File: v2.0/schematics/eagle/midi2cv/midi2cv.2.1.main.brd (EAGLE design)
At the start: 100 x 41.9 mm, 27 parts, among them IC2 PIC18F2431DIP, Q1 20MHz, X1 MAB5SH

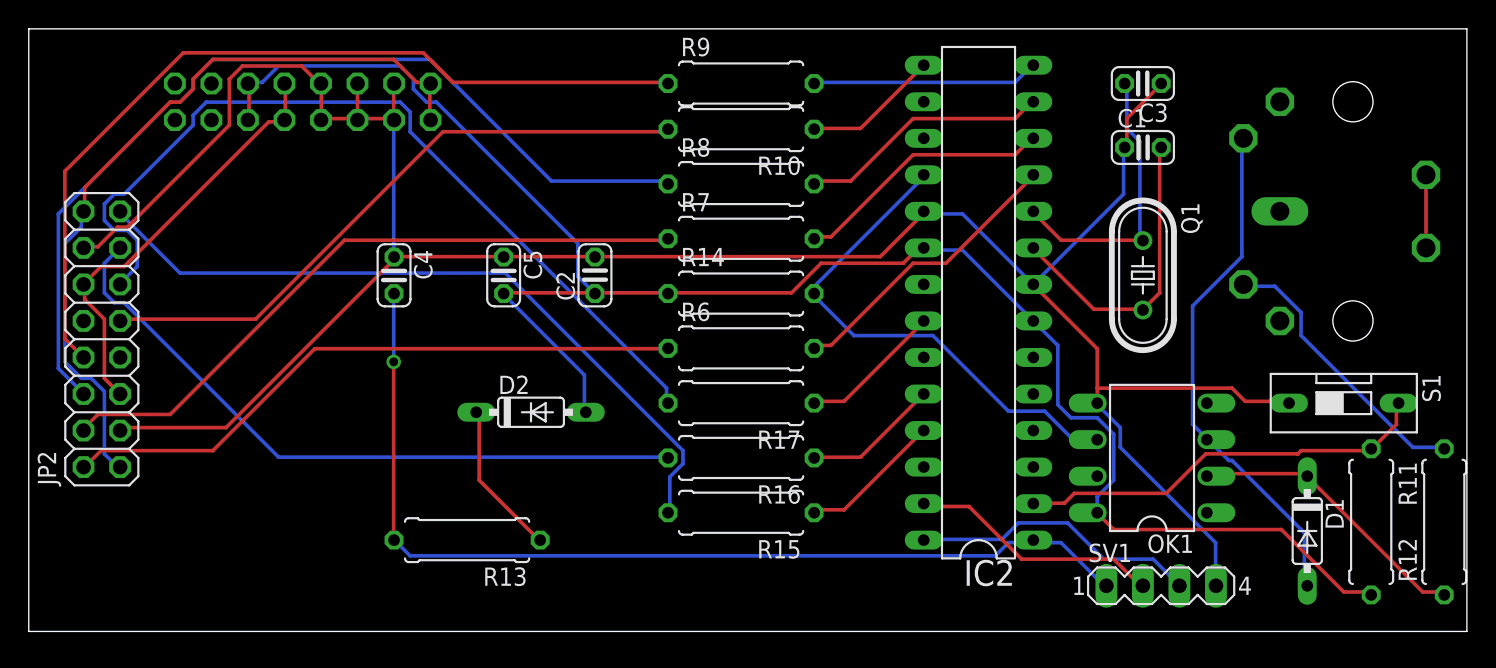
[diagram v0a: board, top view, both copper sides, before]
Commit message: Gerbers generated for midi2cv seeed submission (main and pnl)
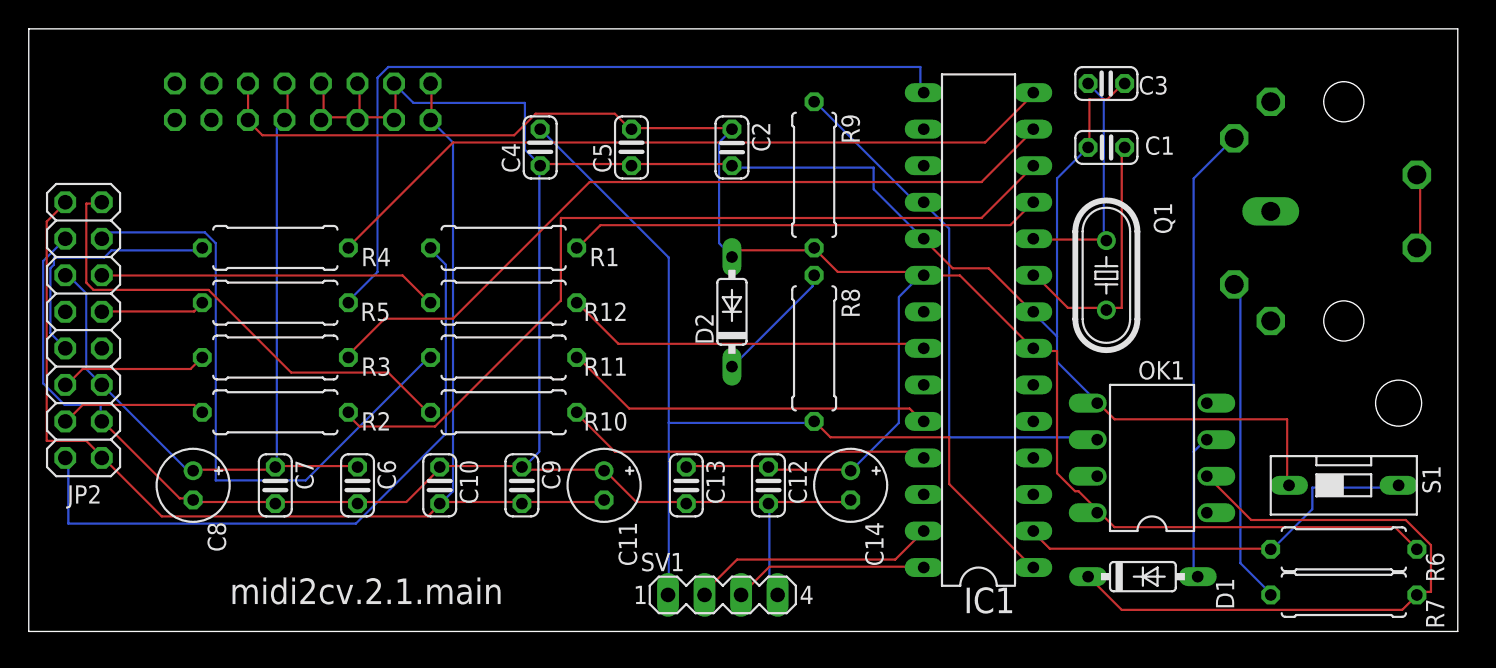
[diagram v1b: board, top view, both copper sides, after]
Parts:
- removed IC2: PIC18F2431DIP, _common:DIL28-3
- removed R13: 10K, _common:0309/10
- removed R14: 360, _common:0309/10
- removed R15, R16, R17: 390, _common:0309/10
- added C10, C13, C7: 0.1uF, _common:C025-024X044
- added C11, C8: 10uF, _common:E2-5
- added C12, C6, C9: 0.01uF, _common:C025-024X044
- added C14: 2.2uF, _common:E2-5
- added IC1: PIC18F2431DIP, _common:DIL28-3
- added R1, R2, R3, R4, R5: 390, _common:0309/10
- R11: value 10K -> 390
- R12: value 220 -> 390
- R6, R8: value 390 -> 10K
- R7: value 390 -> 220
- R9: value 390 -> 360
- moved R12 67.2 mm to (33.0, 22.9), turned to 180 degrees
- moved R11 61.4 mm to (33.0, 19.1), turned to 180 degrees
- moved R7 48.7 mm to (91.4, 2.54), turned to 180 degrees
- moved R6 44.2 mm to (91.4, 5.71)
- moved SV1 30.5 mm to (48.3, 2.54)
- moved R10 25.7 mm to (33.0, 15.2)
- moved D2 15.6 mm to (48.9, 22.2), turned to 90 degrees
- moved C4 13.5 mm to (35.6, 33.7), turned to 90 degrees
- moved C2 13.0 mm to (48.9, 33.7), turned to 270 degrees
- moved C5 12.6 mm to (41.9, 33.7), turned to 90 degrees
- moved R8 12.5 mm to (54.6, 19.7), turned to 270 degrees
- moved D1 11.9 mm to (77.5, 3.81), turned to 0 degrees
- moved R9 8.13 mm to (54.6, 31.8), turned to 90 degrees
- moved S1 5.71 mm to (91.4, 10.2)
- moved C1 2.54 mm to (74.9, 33.7)
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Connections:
- net +12V: now also C6.1, C7.1, C8.+
- net +5V: now also C12.1, C13.1, C14.+, IC1.20, IC1.7, R6.2, R9.1; no longer IC2.20, IC2.7, R11.2, R14.1
- net -12V: now also C10.2, C11.-, C9.2
- net 0V: now also C10.1, C11.+, C12.2, C13.2, C14.-, C6.2, C7.2, C8.-, C9.1, IC1.19, IC1.8; no longer IC2.19, IC2.8
- net CV1: now also R12.2; no longer R17.2
- net CV2: now also R11.2; no longer R16.2
- net CV3: now also R10.2; no longer R15.2
- net GATE1: now also R1.1; no longer R6.1
- net GATE2: now also R2.1; no longer R7.1
- net GATE3: now also R3.1; no longer R8.1
- net GATE4: now also R4.1; no longer R9.1
- net GATE5: now also R5.2; no longer R10.2
- net N$1: now also R8.1; no longer R13.1
- net N$11: now also R7.1; no longer R12.1
- net N$13: now also IC1.18, R9.2; no longer IC2.18, R14.2
- net N$16: now also IC1.25, R10.1; no longer IC2.25, R15.1
- net N$17: now also IC1.24, R11.1; no longer IC2.24, R16.1
- net N$18: now also IC1.22, R12.1; no longer IC2.22, R17.1
- net N$19: now also IC1.15, R5.1; no longer IC2.15, R10.1
- net N$20: now also IC1.2, R6.1; no longer IC2.2, R11.1
- net N$26: now also IC1.11, R1.2; no longer IC2.11, R6.2
- net N$27: now also IC1.9; no longer IC2.9
- net N$28: now also IC1.12, R2.2; no longer IC2.12, R7.2
- net N$29: now also IC1.13, R3.2; no longer IC2.13, R8.2
- net N$30: now also IC1.14, R4.2; no longer IC2.14, R9.2
- net N$6: now also IC1.10; no longer IC2.10
- net N$9: now also R7.2; no longer R12.2
- net PGC: now also IC1.27; no longer IC2.27
- net PGD: now also IC1.28; no longer IC2.28
- net VPP: now also IC1.1, R8.2; no longer IC2.1, R13.2
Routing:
- net GATE3: track 64.1 -> 10.3 mm
- net N$19: track 9.47 -> 56.5 mm
- net GATE4: track 59.7 -> 17.5 mm
- net N$28: track 18.2 -> 59.0 mm
- net 0V: track 176.1 -> 215.3 mm
- net N$29: track 17.7 -> 54.3 mm
- net CV1: track 60.1 -> 23.6 mm
- net GATE5: track 43.7 -> 7.26 mm
- net N$30: track 15.8 -> 52.2 mm
- net GATE2: track 46.2 -> 10.2 mm
- net -12V: track 53.5 -> 89.0 mm
- net +12V: track 29.9 -> 56.5 mm
- net N$11: track 20.1 -> 46.1 mm
- net CV3: track 50.8 -> 34.3 mm
- net N$17: track 9.47 -> 25.9 mm
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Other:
- board size 100 x 41.9 mm -> 99.4 x 41.9 mm
- board text added: "midi2cv.2.1.main"
